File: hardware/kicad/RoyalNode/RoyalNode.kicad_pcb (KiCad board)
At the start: 4 copper layers, 85 x 75 mm, 71 parts, among them J1 XT30PW-M C431092 RC, J2 XT30PW-M C431092 RC, J3 J_LOW_JST_GH_SM02B_GHS_TB_RC, J4 J_LOW_JST_GH_SM02B_GHS_TB_RC, J5 SMA edge envelope, J6 J_LOW_JST_GH_SM04B_GHS_TB_RC, Q1 Infineon PG-DSO-8-27 thermal 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, Q2 Infineon PG-DSO-8-27 thermal 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, Q3 Infineon PG-DSO-8-27 thermal 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, U1 BQ25798 RQM0029A RC, U2 LM66100 DCK0006A SC70-6 RC, U3 TPS61088 RHL0020A thermal via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, U4 LTC4365 TSOT-23-8 RC

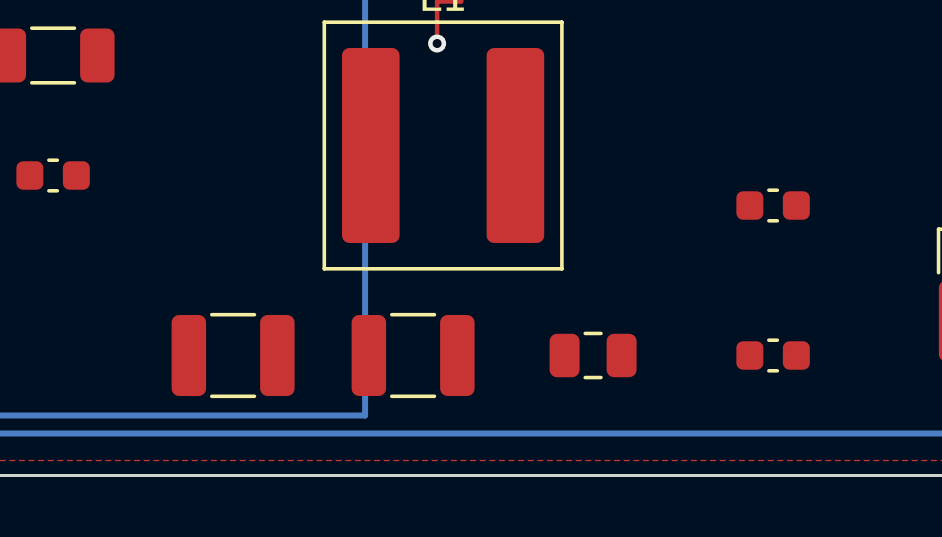
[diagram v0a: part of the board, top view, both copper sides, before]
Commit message: Route radio bulk capacitor bus
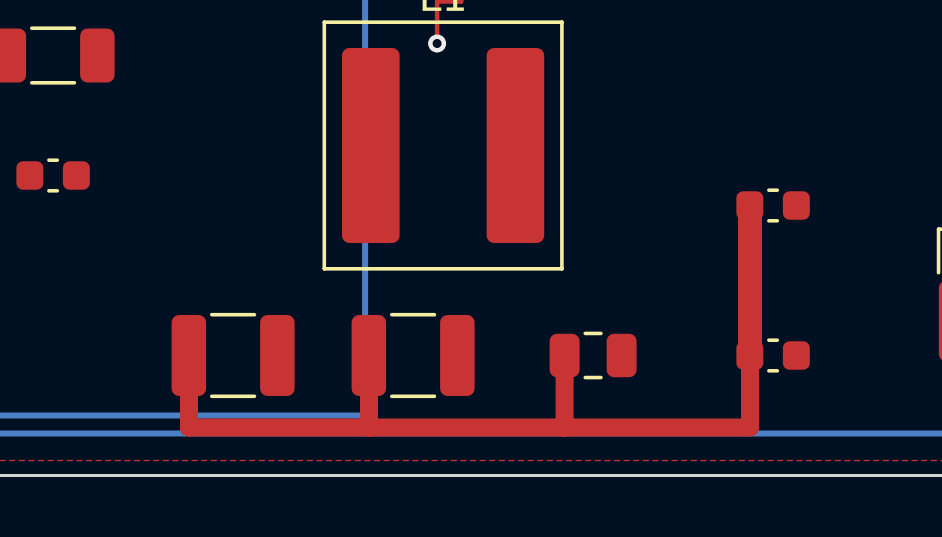
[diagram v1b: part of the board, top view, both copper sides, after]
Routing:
- net 5V_RADIO: track 3.54 -> 41.8 mm

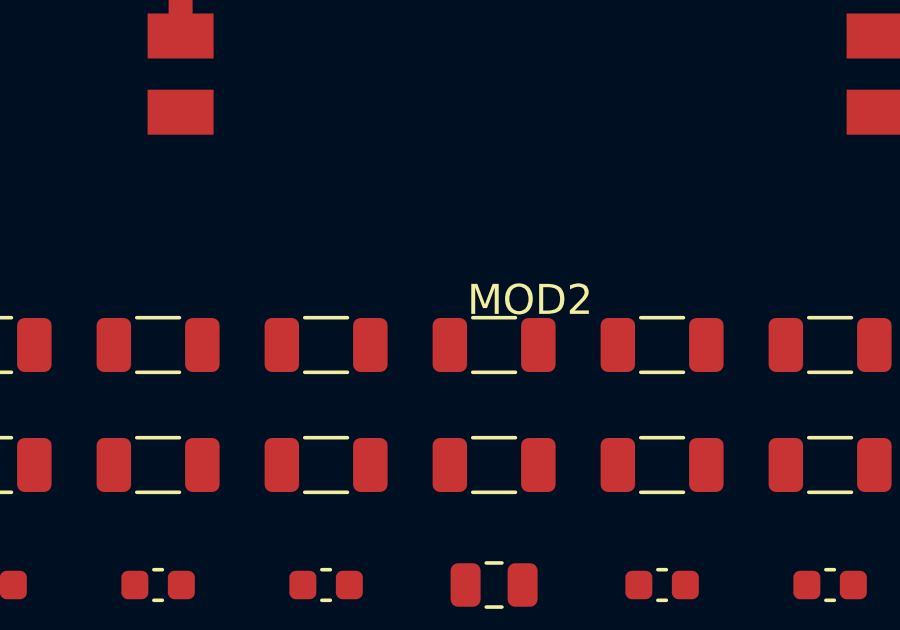
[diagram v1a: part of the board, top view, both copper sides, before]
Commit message: Route BQ PMID capacitor bus
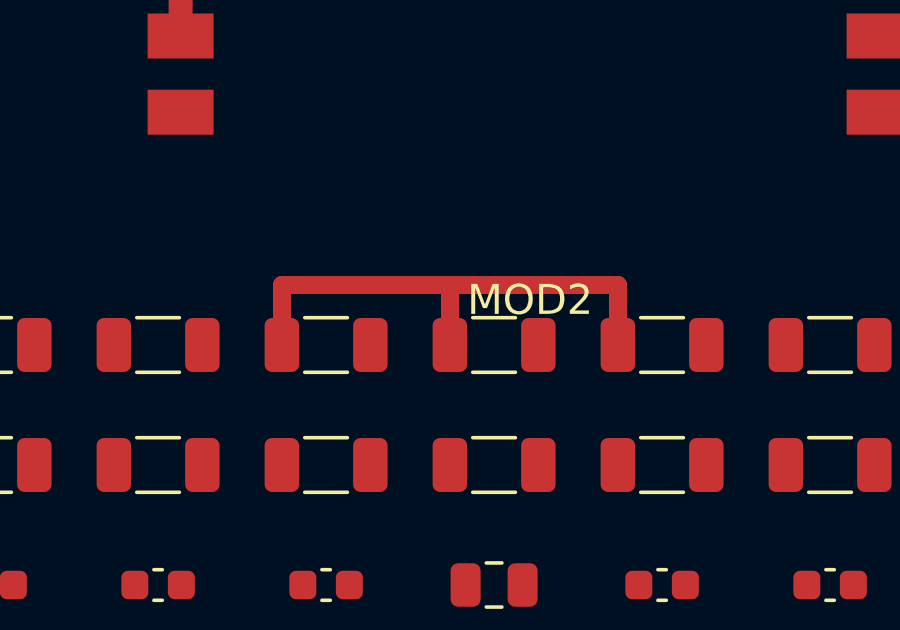
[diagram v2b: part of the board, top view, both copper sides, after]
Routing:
- net BQ_PMID: track 0.00 -> 17.2 mm
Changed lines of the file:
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@@
+	)
+	(segment
+		(start 39.33 75)
+		(end 44.93 75)
+		(width 0.6)
+		(layer "F.Cu")
+		(net "BQ_PMID")
+	)
+	(segment
+		(start 33.73 75)
+		(end 39.33 75)
+		(width 0.6)
+		(layer "F.Cu")
+		(net "BQ_PMID")
+	)
+	(segment
+		(start 33.73 77)
+		(end 33.73 75)
+		(width 0.6)
+		(layer "F.Cu")
+		(net "BQ_PMID")
+	)
+	(segment
+		(start 39.33 77)
+		(end 39.33 75)
+		(width 0.6)
+		(layer "F.Cu")
+		(net "BQ_PMID")
+	)
+	(segment
+		(start 44.93 77)
+		(end 44.93 75)
+		(width 0.6)
+		(layer "F.Cu")
+		(net "BQ_PMID")
 	)
 	(segment

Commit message: Route BQ SYS capacitor bus
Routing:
- net BQ_SYS: track 0.00 -> 28.0 mm
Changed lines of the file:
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@@
+	)
+	(segment
+		(start 33.73 81)
+		(end 33.73 83.4)
+		(width 0.6)
+		(layer "F.Cu")
+		(net "BQ_SYS")
+	)
+	(segment
+		(start 39.33 81)
+		(end 39.33 83.4)
+		(width 0.6)
+		(layer "F.Cu")
+		(net "BQ_SYS")
+	)
+	(segment
+		(start 28.13 83.4)
+		(end 33.73 83.4)
+		(width 0.6)
+		(layer "F.Cu")
+		(net "BQ_SYS")
+	)
+	(segment
+		(start 34.43 85)
+		(end 34.43 83.4)
+		(width 0.6)
+		(layer "F.Cu")
+		(net "BQ_SYS")
+	)
+	(segment
+		(start 22.53 81)
+		(end 22.53 83.4)
+		(width 0.6)
+		(layer "F.Cu")
+		(net "BQ_SYS")
+	)
+	(segment
+		(start 28.13 81)
+		(end 28.13 83.4)
+		(width 0.6)
+		(layer "F.Cu")
+		(net "BQ_SYS")
+	)
+	(segment
+		(start 33.73 83.4)
+		(end 39.33 83.4)
+		(width 0.6)
+		(layer "F.Cu")
+		(net "BQ_SYS")
+	)
+	(segment
+		(start 22.53 83.4)
+		(end 28.13 83.4)
+		(width 0.6)
+		(layer "F.Cu")
+		(net "BQ_SYS")
 	)
 	(segment

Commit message: Route BQ VBUS capacitor pair
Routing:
- net BQ_VBUS: track 14.1 -> 23.7 mm
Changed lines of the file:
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@@
+	)
+	(segment
+		(start 22.53 75)
+		(end 28.13 75)
+		(width 0.6)
+		(layer "F.Cu")
+		(net "BQ_VBUS")
 	)
 	(segment
@@
 		(width 0.6)
 		(layer "F.Cu")
+		(net "BQ_VBUS")
+	)
+	(segment
+		(start 28.13 77)
+		(end 28.13 75)
+		(width 0.6)
+		(layer "F.Cu")
+		(net "BQ_VBUS")
+	)
+	(segment
+		(start 22.53 77)
+		(end 22.53 75)
+		(width 0.6)
+		(layer "F.Cu")

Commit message: Route BAT RAW capacitor pair
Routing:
- net BAT_RAW: track 0.40 -> 10.8 mm
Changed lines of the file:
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@@
+	)
+	(segment
+		(start 44.93 83.4)
+		(end 50.53 83.4)
+		(width 0.6)
+		(layer "F.Cu")
+		(net "BAT_RAW")
+	)
+	(segment
+		(start 50.53 81)
+		(end 50.53 83.4)
+		(width 0.6)
+		(layer "F.Cu")
+		(net "BAT_RAW")
 	)
 	(segment
@@
 		(layer "F.Cu")
 		(net "BAT_RAW")
+	)
+	(segment
+		(start 44.93 81)
+		(end 44.93 83.4)
+		(width 0.6)
+		(layer "F.Cu")
+		(net "BAT_RAW")

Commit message: Route upper boost capacitor pairs
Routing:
- net 5V_RADIO: track 41.8 -> 51.4 mm
- net BQ_SYS: track 28.0 -> 37.6 mm
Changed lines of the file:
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@@
+	)
+	(segment
+		(start 23.03 24.5)
+		(end 23.03 22.5)
+		(width 0.4)
+		(layer "F.Cu")
+		(net "BQ_SYS")
 	)
 	(segment
@@
 	)
 	(segment
+		(start 23.03 22.5)
+		(end 28.63 22.5)
+		(width 0.4)
+		(layer "F.Cu")
+		(net "BQ_SYS")
+	)
+	(segment
 		(start 33.73 83.4)
 		(end 39.33 83.4)
@@
 		(end 28.13 83.4)
 		(width 0.6)
+		(layer "F.Cu")
+		(net "BQ_SYS")
+	)
+	(segment
+		(start 28.63 22.5)
+		(end 28.63 24.5)
+		(width 0.4)
 		(layer "F.Cu")
 		(net "BQ_SYS")
@@
 	)
 	(segment
+		(start 34.23 22.5)
+		(end 39.83 22.5)
+		(width 0.4)
+		(layer "F.Cu")
+		(net "5V_RADIO")
+	)
+	(segment
+		(start 34.23 24.5)
+		(end 34.23 22.5)
+		(width 0.4)
+		(layer "F.Cu")
+		(net "5V_RADIO")
+	)
+	(segment
 		(start 62.53 91)
 		(end 62.53 93.4)
@@
 		(layer "F.Cu")
 		(net "5V_RADIO")
+	)
+	(segment
+		(start 39.83 22.5)
+		(end 39.83 24.5)
+		(width 0.4)
+		(layer "F.Cu")
+		(net "5V_RADIO")

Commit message: Route boost feedback divider link
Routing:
- net BOOST_FB: track 0.00 -> 3.95 mm
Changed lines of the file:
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@@
+	)
+	(segment
+		(start 42.13 29)
+		(end 46.08 29)
+		(width 0.2)
+		(layer "F.Cu")
+		(net "BOOST_FB")
 	)
 	(segment

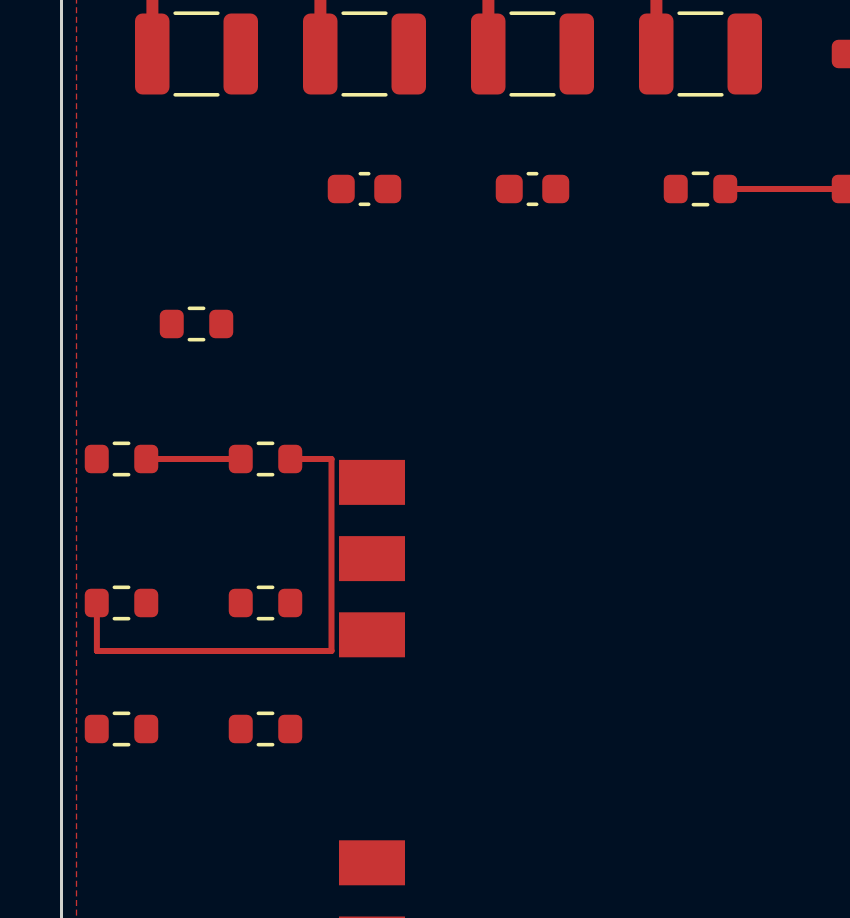
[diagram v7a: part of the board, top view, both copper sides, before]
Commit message: Route boost compensation RC link
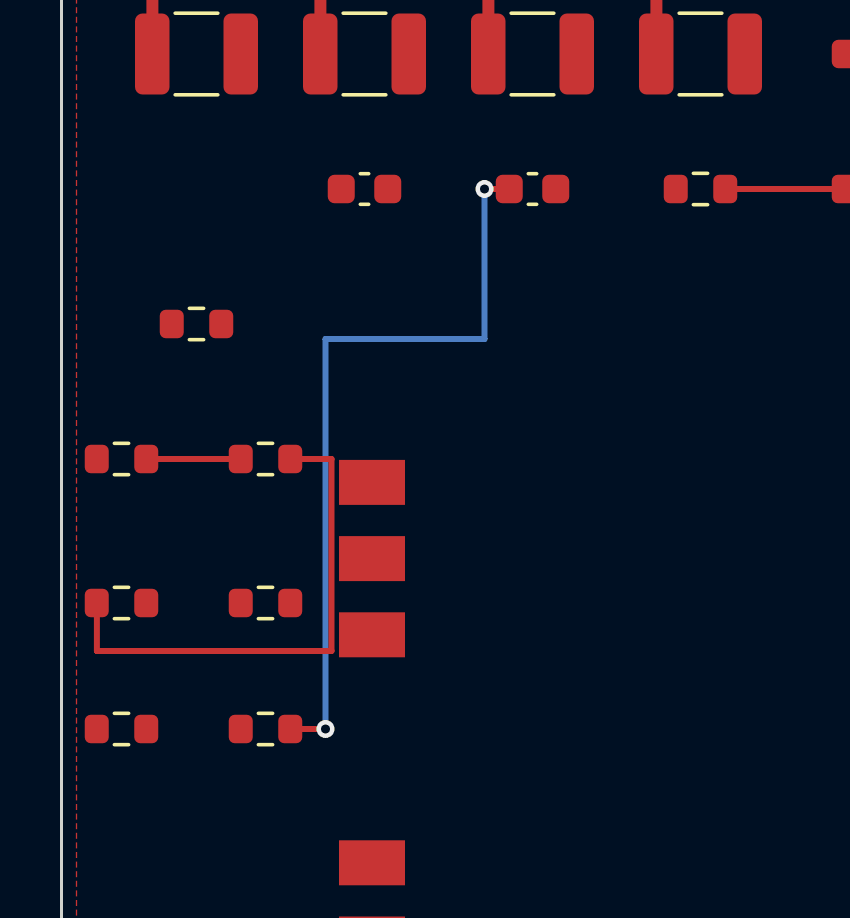
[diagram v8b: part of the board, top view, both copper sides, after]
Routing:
- net BOOST_COMP_RC: track 0.00 -> 25.3 mm, vias 0 -> 2
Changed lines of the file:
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@@
+	)
+	(segment
+		(start 34.1 29)
+		(end 34.93 29)
+		(width 0.2)
+		(layer "F.Cu")
+		(net "BOOST_COMP_RC")
+	)
+	(segment
+		(start 27.63 47)
+		(end 28.8 47)
+		(width 0.2)
+		(layer "F.Cu")
+		(net "BOOST_COMP_RC")
+	)
+	(via
+		(at 34.1 29)
+		(size 0.6)
+		(drill 0.3)
+		(layers "F.Cu" "B.Cu")
+		(net "BOOST_COMP_RC")
+	)
+	(via
+		(at 28.8 47)
+		(size 0.6)
+		(drill 0.3)
+		(layers "F.Cu" "B.Cu")
+		(net "BOOST_COMP_RC")
+	)
+	(segment
+		(start 34.1 34)
+		(end 34.1 29)
+		(width 0.2)
+		(layer "B.Cu")
+		(net "BOOST_COMP_RC")
+	)
+	(segment
+		(start 28.8 47)
+		(end 28.8 34)
+		(width 0.2)
+		(layer "B.Cu")
+		(net "BOOST_COMP_RC")
+	)
+	(segment
+		(start 28.8 34)
+		(end 34.1 34)
+		(width 0.2)
+		(layer "B.Cu")
+		(net "BOOST_COMP_RC")
 	)
 	(segment
